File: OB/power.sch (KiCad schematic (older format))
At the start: 24 parts, among them U1 V3S

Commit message: Progress on wifi
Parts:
- removed U?: EA3036, symbol ob:EA3036
- added C? (x4): 220pF, symbol Device:C
- added C? (x4): 22uF, symbol Device:C
- added C? (x4): 10uF, symbol Device:C
- added L? (x4): 2.2 uH, symbol Device:L
- added R? (x3): 150K, symbol Device:R
- added R?: 200K, symbol Device:R
- added R? (x2): 100K, symbol Device:R
- added R?: 360K, symbol Device:R
- added R?: 680K, symbol Device:R
- added U?: EA3058, symbol EA3058:EA3058
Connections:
- net labels added: +2V8, +BATT
- net labels removed: USB_DRVVBUS, VBAT
- wire segments 64 -> 114
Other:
- moved on the sheet: C54, C55, C56, C57, C63, C64, C65, R31, R32

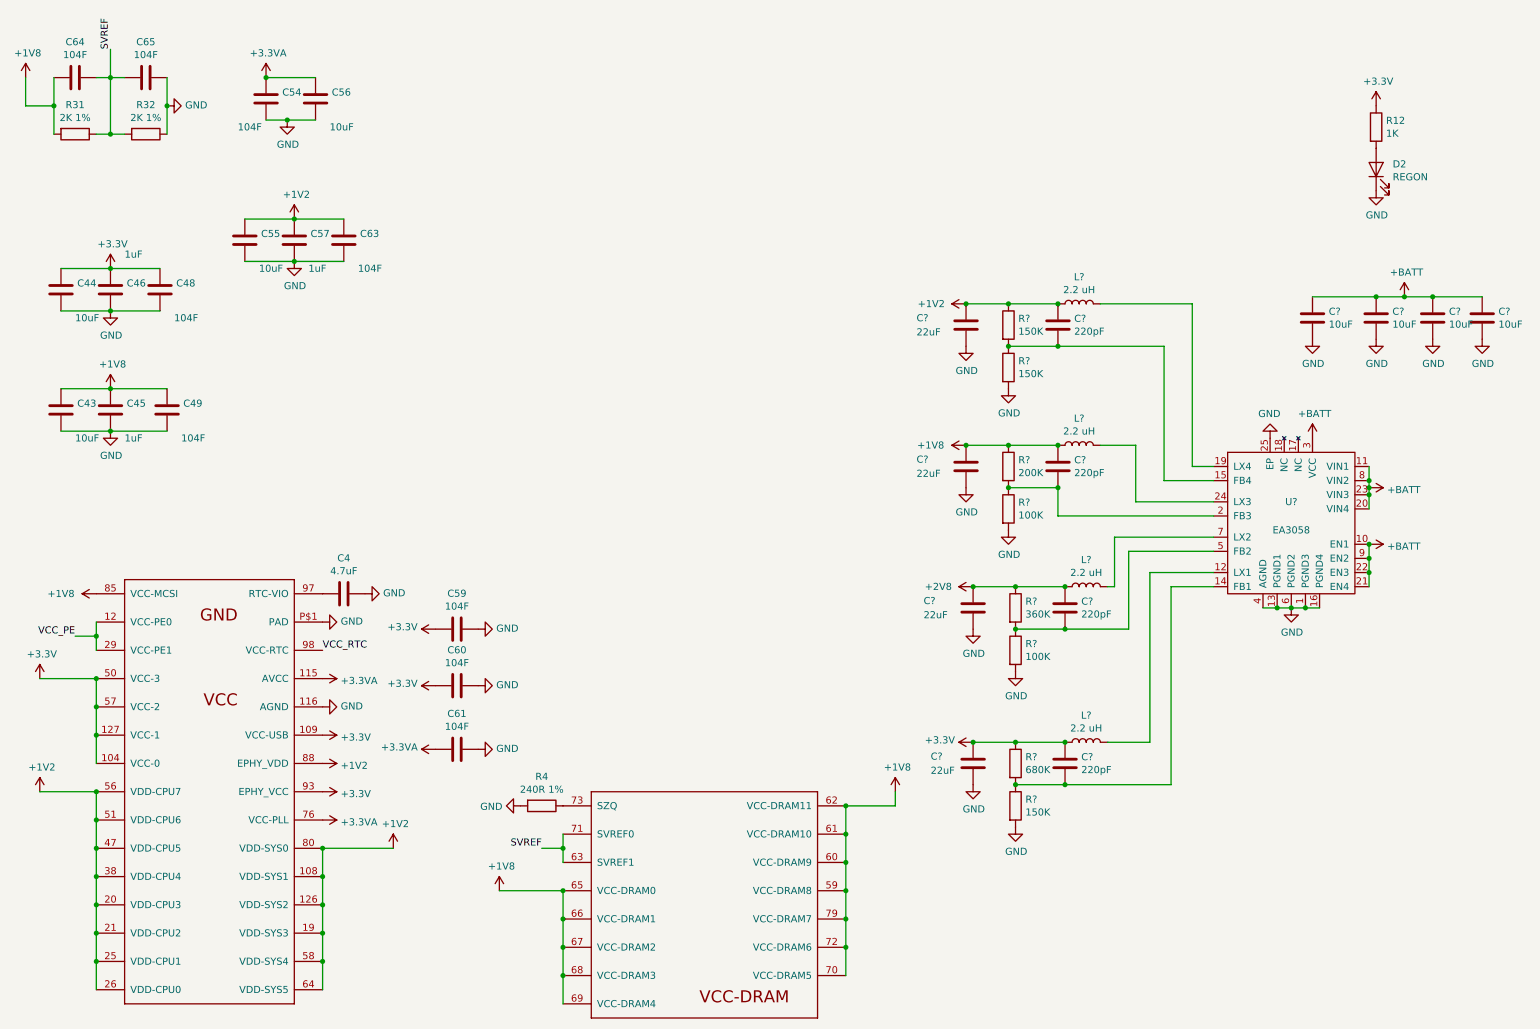
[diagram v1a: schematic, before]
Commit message: +esp32picod4 +fix mounting hole position -ceramic antenna +ufl -spi flash
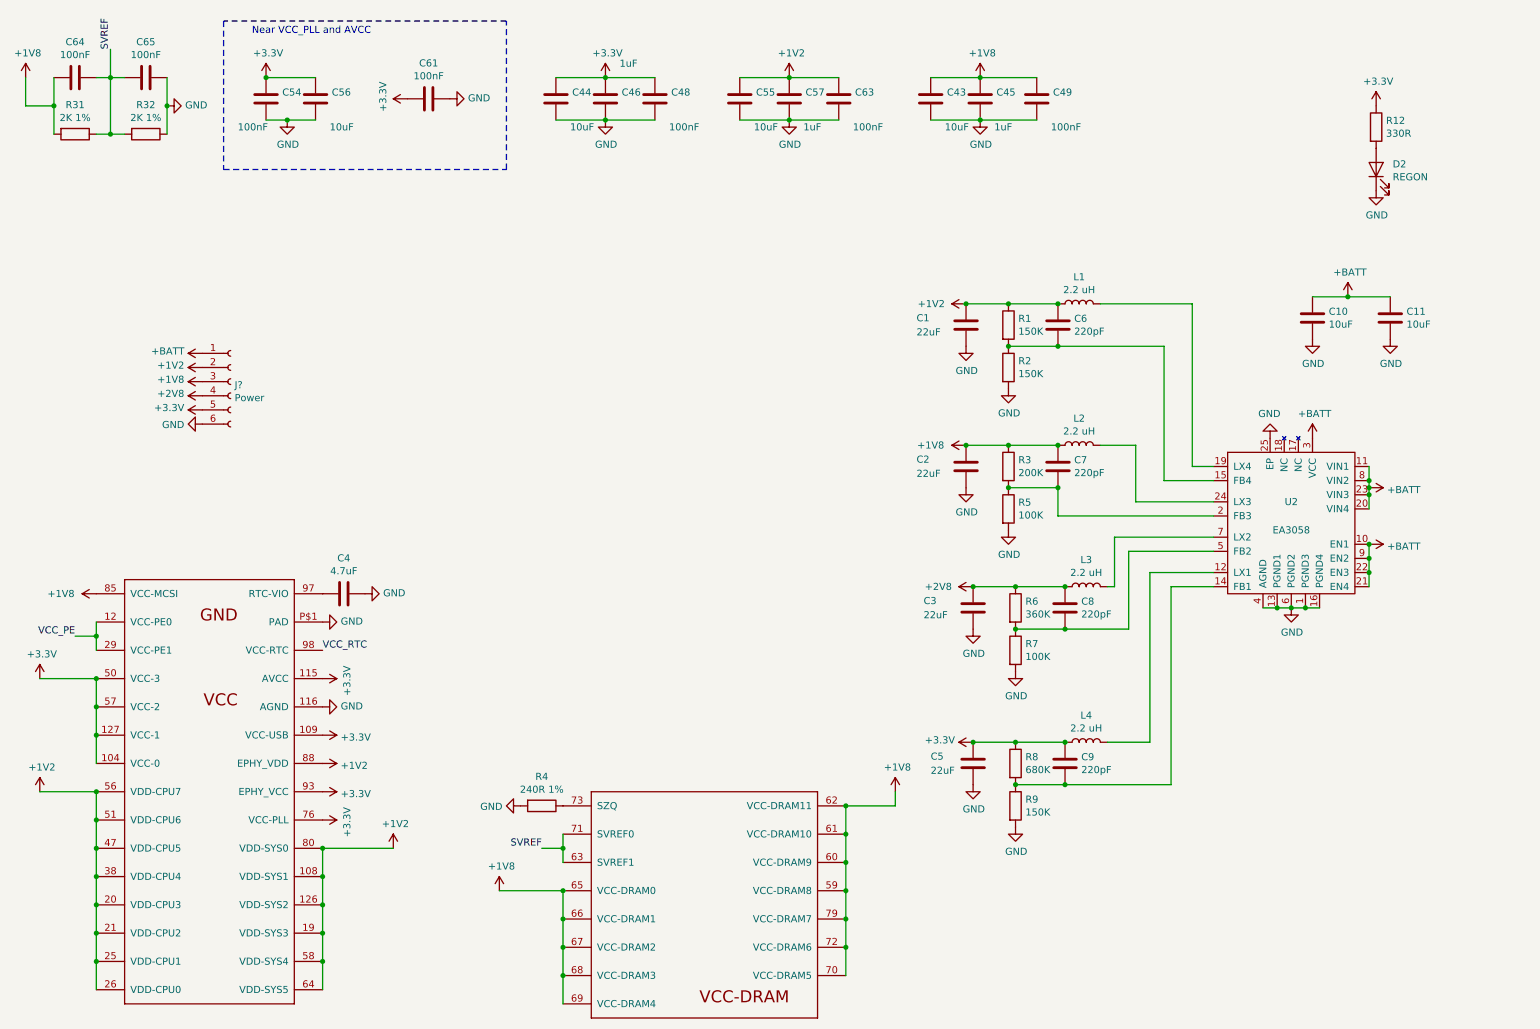
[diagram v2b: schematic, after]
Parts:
- removed C59, C60: 104F, Capacitor_SMD:C_0402_1005Metric, symbol Device:C
- removed C? (x2): 10uF, symbol Device:C
- added J?: Power, symbol Connector:Conn_01x06_Female
- C1, C10, C11, C2, C3, C5, C6, C7, C8, C9: renamed from C?; footprint (none) -> Capacitor_SMD:C_0402_1005Metric
- C43, C44, C55, C56: footprint Capacitor_SMD:C_0603_1608Metric -> Capacitor_SMD:C_0402_1005Metric
- C48, C49, C54, C61, C63, C64, C65: value 104F -> 100nF
- L1, L2, L3, L4: renamed from L?; footprint (none) -> Inductor_SMD:L_0201_0603Metric
- R1, R2, R3, R5, R6, R7, R8, R9: renamed from R?; footprint (none) -> Resistor_SMD:R_0402_1005Metric
- R12: value 1K -> 330R
- gave numbers to parts that had none: 1
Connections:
- net +3.3VA is gone; now on net +3V3: C54.1, C56.1, C61.2, U1.115 (AVCC), U1.76 (VCC-PLL)
- net +1V2: now also J?.2 (Pin_2)
- net +1V8: now also J?.3 (Pin_3)
- net +2V8: now also J?.4 (Pin_4)
- net +3V3: now also J?.5 (Pin_5)
- net +BATT: now also J?.1 (Pin_1)
- net GND: now also J?.6 (Pin_6)
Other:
- note added: "Near VCC_PLL and AVCC"
- moved on the sheet: C11, C43, C44, C45, C46, C48, C49, C55, C57, C61, C63
